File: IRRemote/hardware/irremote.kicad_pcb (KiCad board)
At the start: 2 copper layers, 52.1 x 29.8 mm, 34 parts, among them P2 TL1838_PINHEADER, P3 DS18B20_PINHEADER_TO92, P4 CONN_02X04, P5 CONN_01X04, P6 CONN_01X05, P7 CONN_01X04, P8 TEMP6000, P9 CONN_01X02, Q1 Q_NPN_BEC (MMBT2222ALT1G, 145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, Q2 Q_NPN_BEC (MMBT2222ALT1G, 145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

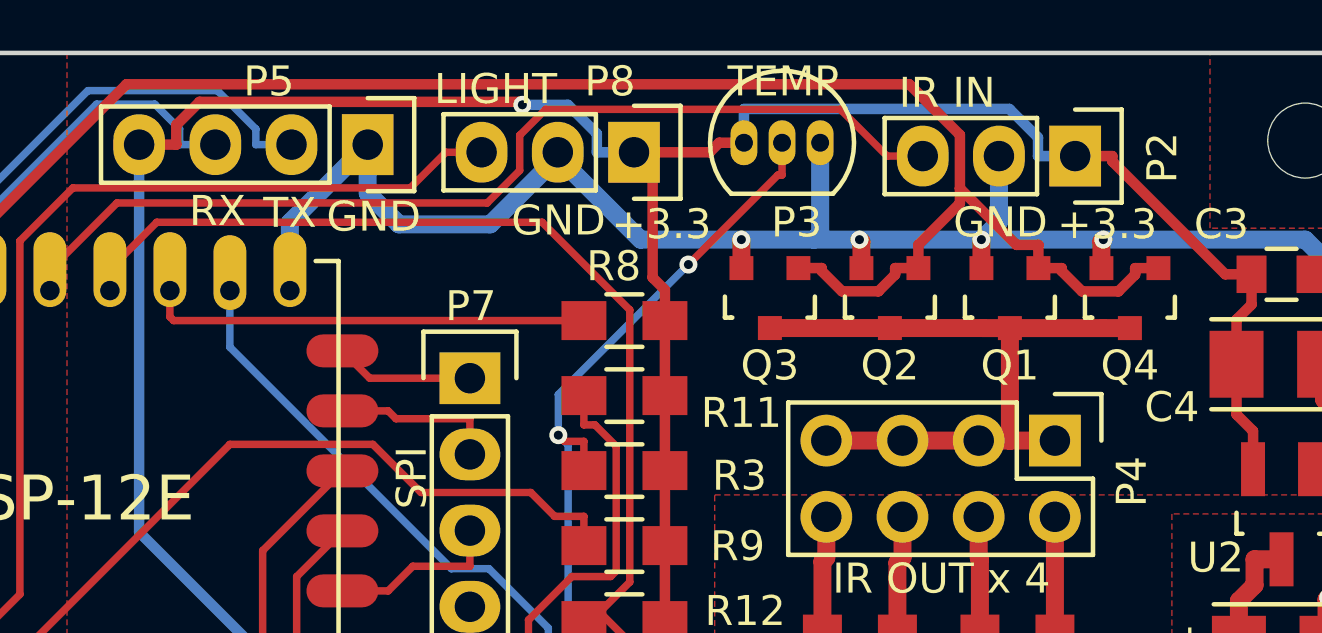
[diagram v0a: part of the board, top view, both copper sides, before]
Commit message: beefed up the led connections a bit
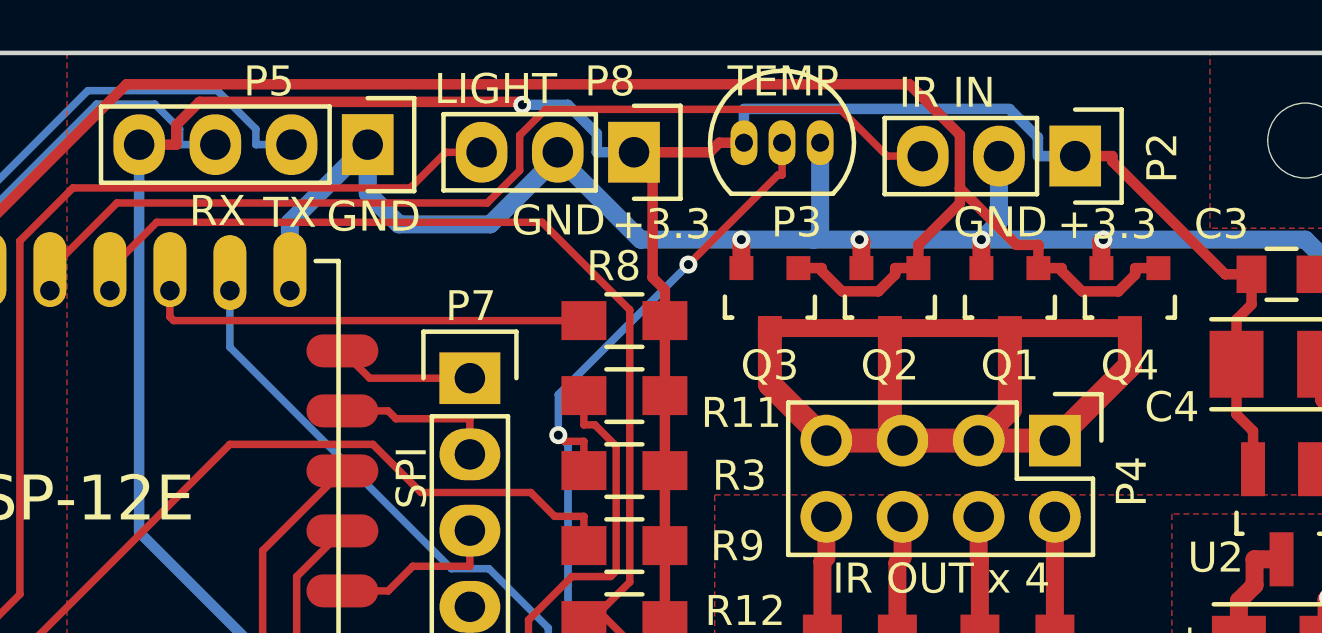
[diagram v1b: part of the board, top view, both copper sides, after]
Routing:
- net LED_DR_5: track 23.4 -> 37.0 mm
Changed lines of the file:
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@@
     (thickness 1.6)
     (drawings 31)
-    (tracks 307)
+    (tracks 313)
     (zones 0)
     (modules 34)
@@
   )
   (setup
-    (last_trace_width 0.25)
+    (last_trace_width 0.8)
     (user_trace_width 0.2)
     (user_trace_width 0.3)
@@
     (effects (font (size 1 1) (thickness 0.25)))
   )
-  (gr_text GND (at 146.685 58.2295 360) (layer F.SilkS)
+  (gr_text GND (at 146.685 58.2295) (layer F.SilkS)
     (effects (font (size 1 1) (thickness 0.25)))
   )
@@
     (effects (font (size 1 1) (thickness 0.25)))
   )
-  (gr_text GND (at 125.7935 58.039 360) (layer F.SilkS)
+  (gr_text GND (at 125.7935 58.039) (layer F.SilkS)
     (effects (font (size 1 1) (thickness 0.25)))
   )
@@
     (effects (font (size 1 1) (thickness 0.25)))
   )
-  (gr_text TX (at 122.9995 57.912 360) (layer F.SilkS)
+  (gr_text TX (at 122.9995 57.912) (layer F.SilkS)
     (effects (font (size 1 1) (thickness 0.25)))
   )
-  (gr_text RX (at 120.5865 57.8485 360) (layer F.SilkS)
+  (gr_text RX (at 120.5865 57.8485) (layer F.SilkS)
     (effects (font (size 1 1) (thickness 0.25)))
   )
@@
   (segment (start 145.334 57.0915) (end 147.2182 58.9757) (width 0.35) (layer F.Cu) (net 6))
   (segment (start 147.95 59.751) (end 147.95 58.9757) (width 0.35) (layer F.Cu) (net 6))
+  (segment (start 139 61.74822) (end 139 63.62) (width 0.8) (layer F.Cu) (net 7))
+  (segment (start 139 63.62) (end 140.88 65.5) (width 0.8) (layer F.Cu) (net 7))
+  (segment (start 151 61.75002) (end 151 63) (width 0.8) (layer F.Cu) (net 7))
+  (segment (start 151 63) (end 148.5 65.5) (width 0.8) (layer F.Cu) (net 7))
+  (segment (start 145.96 65.5) (end 148.5 65.5) (width 0.8) (layer F.Cu) (net 7))
+  (segment (start 143.42 65.5) (end 145.96 65.5) (width 0.8) (layer F.Cu) (net 7))
+  (segment (start 140.88 65.5) (end 143.42 65.5) (width 0.8) (layer F.Cu) (net 7))
+  (segment (start 143 61.74822) (end 143 65.08) (width 0.8) (layer F.Cu) (net 7))
+  (segment (start 143 65.08) (end 143.42 65.5) (width 0.8) (layer F.Cu) (net 7))
+  (segment (start 147 61.75002) (end 147 64.46) (width 0.8) (layer F.Cu) (net 7))
+  (segment (start 147 64.46) (end 145.96 65.5) (width 0.8) (layer F.Cu) (net 7))
   (segment (start 139 61.7482) (end 143 61.7482) (width 0.6) (layer F.Cu) (net 7))
   (segment (start 146.0978 61.7482) (end 146.0996 61.75) (width 0.6) (layer F.Cu) (net 7))
   (segment (start 143 61.7482) (end 146.0978 61.7482) (width 0.6) (layer F.Cu) (net 7))
   (segment (start 147 61.75) (end 146.0996 61.75) (width 0.6) (layer F.Cu) (net 7))
-  (segment (start 145.96 65.5) (end 147 65.5) (width 0.6) (layer F.Cu) (net 7))
-  (segment (start 147 65.5) (end 148.5 65.5) (width 0.6) (layer F.Cu) (net 7))
-  (segment (start 147 65.5) (end 147 61.75) (width 0.6) (layer F.Cu) (net 7))
   (segment (start 151 61.75) (end 150.0996 61.75) (width 0.6) (layer F.Cu) (net 7))
   (segment (start 147 61.75) (end 150.0996 61.75) (width 0.6) (layer F.Cu) (net 7))
-  (segment (start 140.88 65.5) (end 143.42 65.5) (width 0.6) (layer F.Cu) (net 7))
-  (segment (start 143.42 65.5) (end 145.96 65.5) (width 0.6) (layer F.Cu) (net 7))
   (segment (start 148.5 68.04) (end 148.5 72.05) (width 0.6) (layer F.Cu) (net 8))
   (segment (start 146 69.4439) (end 146 72.05) (width 0.6) (layer F.Cu) (net 9))

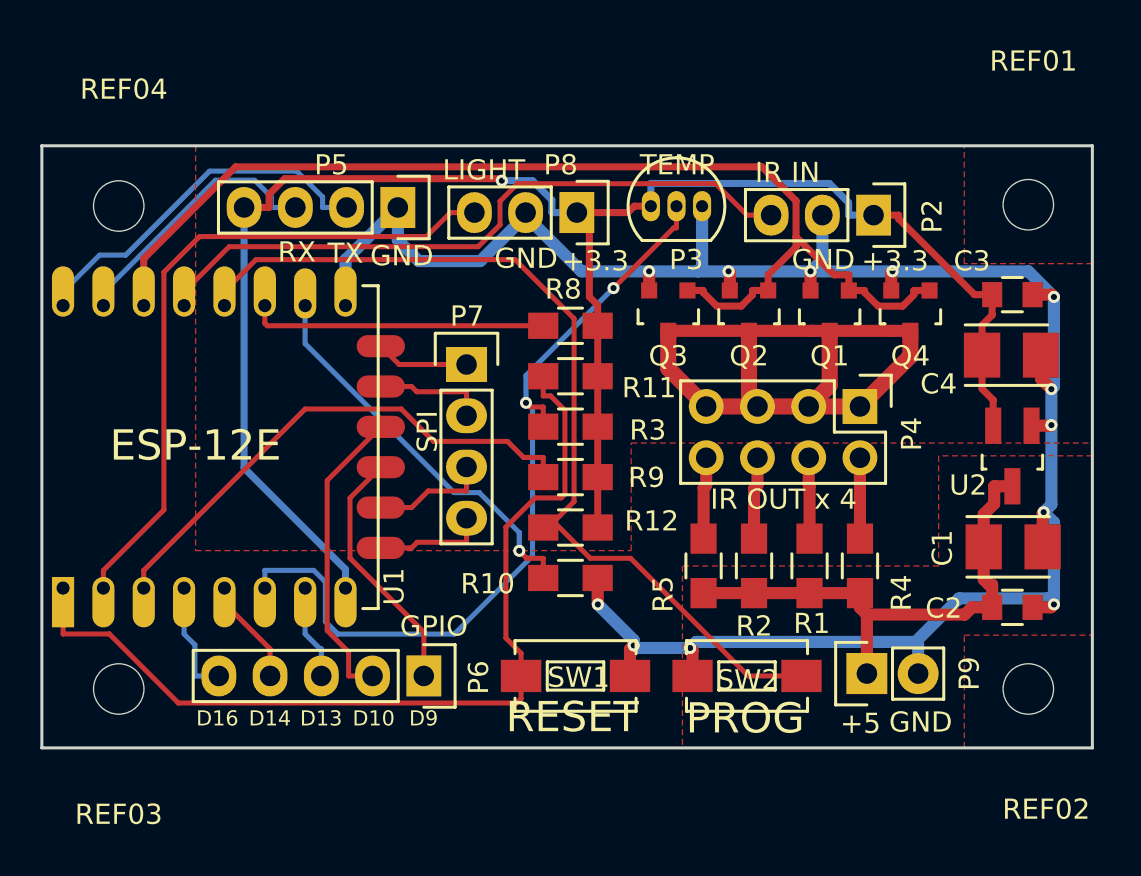
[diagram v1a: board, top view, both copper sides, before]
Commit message: updated board for correct SMD push buttons
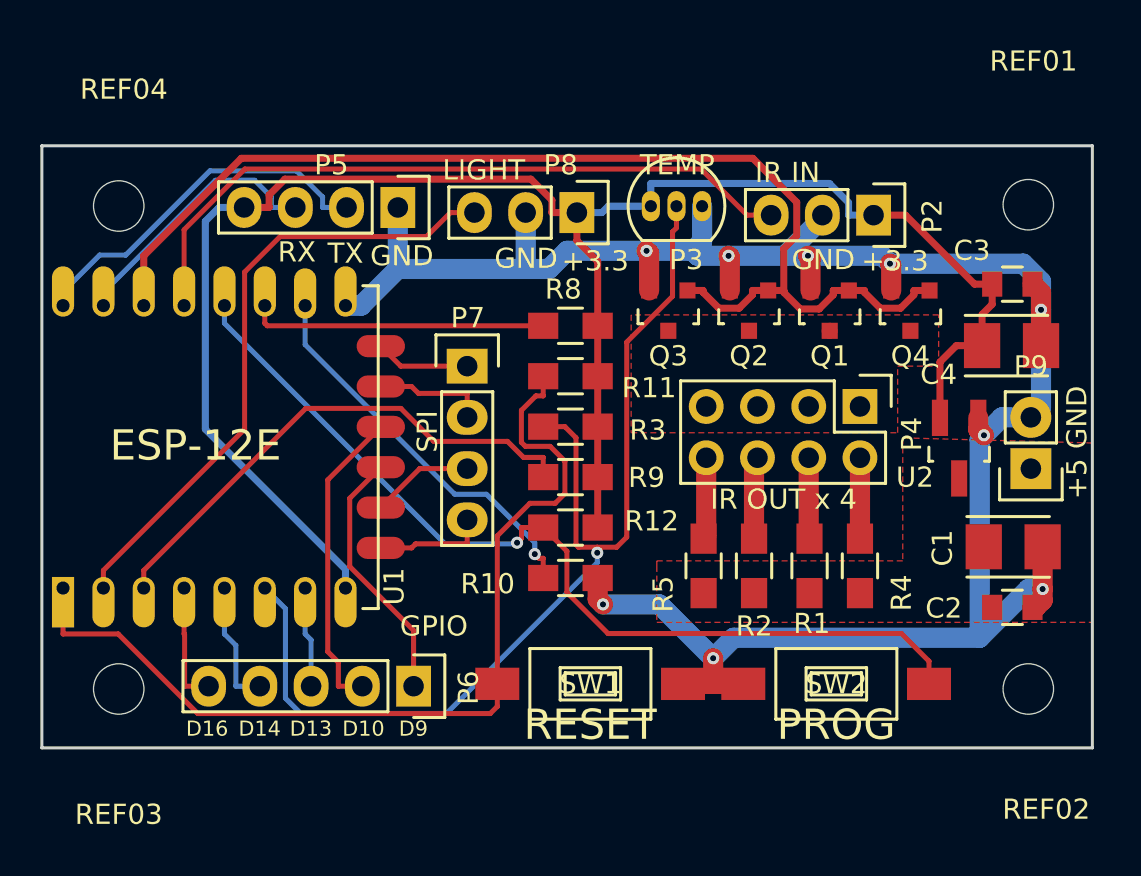
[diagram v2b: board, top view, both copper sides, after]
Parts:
- SW1, SW2: footprint Buttons_Switches_SMD:SW_SPST_EVQPE1 -> Buttons_Switches_SMD:SW_SPST_FSMSM
- moved P9 13.0 mm to (157.0, 68.6), turned to 180 degrees
- moved SW2 4.44 mm to (147.3, 79.2)
- moved U2 2.67 mm to (153.4, 67.6)
- moved SW1 0.82 mm to (135.1, 79.2)
- moved P6 0.72 mm to (126.4, 79.4)
- moved C3 0.52 mm to (156.1, 59.4)
- moved C4 0.47 mm to (156.0, 62.5)
- moved P7 0.09 mm to (129.0, 63.5)
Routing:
- net LED_DR_5: track 37.0 -> 0.00 mm
- net +5V: track 25.6 -> 0.00 mm
- net TEMP_READ: track 40.8 -> 52.9 mm, vias 2 -> 1
- net GND: track 106.7 -> 111.4 mm, vias 12 -> 9
- net +3V3: track 86.8 -> 90.5 mm, vias 1 -> 0
- net TEMT: track 33.5 -> 31.2 mm
- net IR_IN: track 33.3 -> 35.0 mm
- net LED_DR: track 56.1 -> 57.1 mm
- net Net-(P6-Pad4): track 5.29 -> 6.29 mm
- net Net-(R8-Pad1): track 45.4 -> 46.3 mm
- net Net-(R12-Pad2): track 46.8 -> 46.0 mm, vias 0 -> 1
- net Net-(P7-Pad3): track 5.78 -> 5.08 mm
- added copper zone on F.Cu, net LED_DR_5
- removed copper zone on F.Cu, net +3V3

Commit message: moved the microusb for power, fixed push button switches, flipped IR receiver
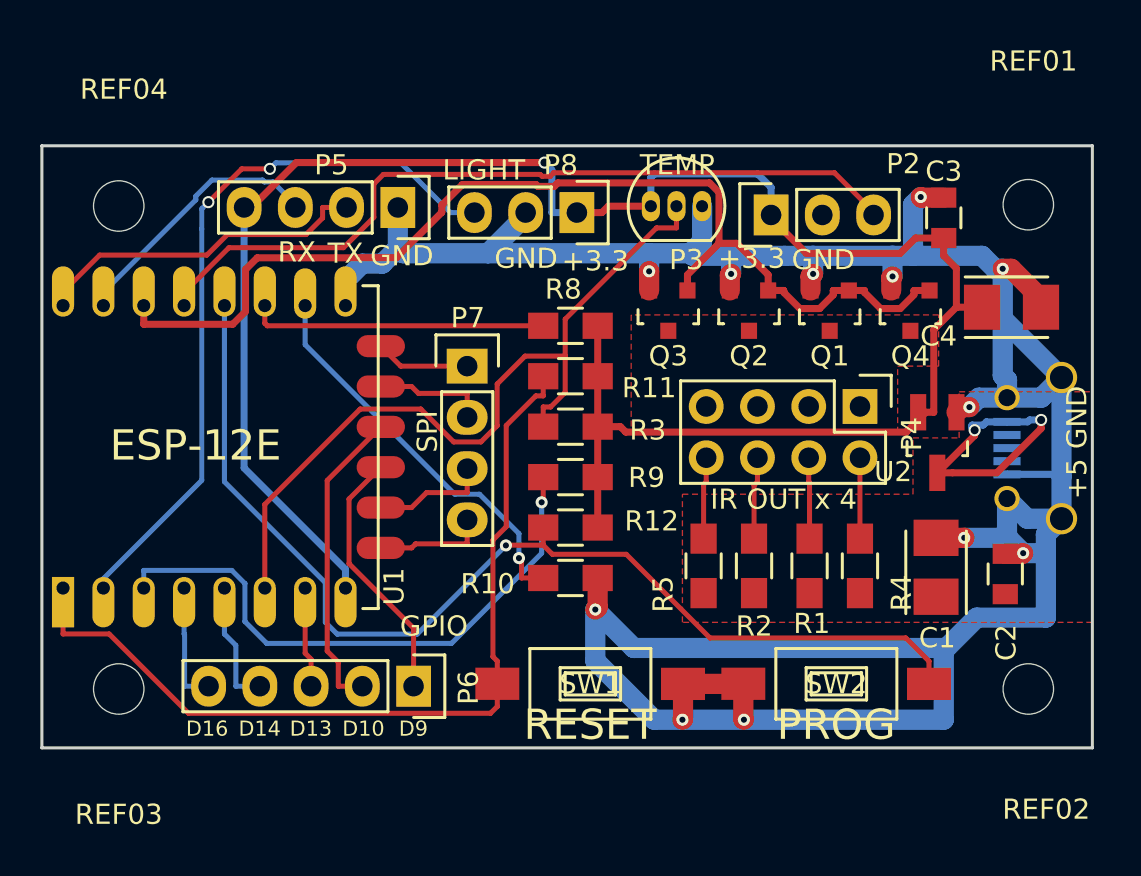
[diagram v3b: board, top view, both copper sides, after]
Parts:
- removed P9: CONN_01X02, Pin_Headers:Pin_Header_Straight_1x02
- added P1: USB_OTG, MyKiCadLibs:USB_Micro-B-OshPark, B.Cu at (157.4, 67.6)
- moved P2 5.08 mm to (144.1, 56.0), turned to 90 degrees
- moved C3 4.73 mm to (152.7, 56.1), turned to 90 degrees
- moved C1 3.95 mm to (152.3, 73.5), turned to 90 degrees
- moved C4 1.91 mm to (156.0, 60.6)
- moved C2 1.69 mm to (155.7, 73.8), turned to 90 degrees
- moved U2 1.12 mm to (152.3, 67.3)
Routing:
- net GND: track 111.4 -> 156.5 mm, vias 9 -> 12
- net TEMP_READ: track 52.9 -> 39.1 mm, vias 1 -> 0
- net +5V: track 0.00 -> 13.7 mm, vias 0 -> 2
- net +3V3: track 90.5 -> 101.5 mm, vias 0 -> 1
- net Net-(R12-Pad2): track 46.0 -> 54.1 mm
- net TEMT: track 31.2 -> 36.3 mm, vias 0 -> 2
- net IR_IN: track 35.0 -> 39.3 mm
- net LED_DR: track 57.1 -> 53.3 mm
- net Net-(R8-Pad1): track 46.3 -> 43.3 mm
- net Net-(R9-Pad1): track 26.0 -> 28.9 mm, vias 0 -> 1
- net RXD_UA_1: track 18.3 -> 16.8 mm
- net Net-(P7-Pad3): track 5.08 -> 5.78 mm
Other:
- board text removed: "IR IN"

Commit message: update oshpark link
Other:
- board text added: "IR In"
- board text removed: "+5"
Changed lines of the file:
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@@
     (links 77)
     (no_connects 0)
-    (area 89.666424 39.630625 175.259 86.7)
+    (area 89.666424 42.87 175.259 86.7)
     (thickness 1.6)
-    (drawings 30)
+    (drawings 29)
     (tracks 364)
     (zones 0)
@@
     (descr "Through hole pin header")
     (tags "pin header")
-    (fp_text reference P2 (at 2.531 6.554 180) (layer F.SilkS)
+    (fp_text reference P2 (at -0.635 7.035 270) (layer F.SilkS)
       (effects (font (size 1 1) (thickness 0.15)))
     )
@@
       (net 1 GND))
   )
+  (gr_text "IR In" (at 149.225 53.721) (layer F.SilkS)
+    (effects (font (size 1 1) (thickness 0.25)))
+  )
   (dimension 52.07 (width 0.3) (layer Cmts.User)
     (gr_text "52.070 mm" (at 133.985 44.37) (layer Cmts.User)
@@
     (effects (font (size 1 1) (thickness 0.25)))
   )
-  (gr_text TEMP (at 139.446 53.5305) (layer F.SilkS)
+  (gr_text TEMP (at 139.446 53.721) (layer F.SilkS)
     (effects (font (size 1 1) (thickness 0.25)))
   )
-  (gr_text GND (at 159.258 66.04 90) (layer F.SilkS)
-    (effects (font (size 1 1) (thickness 0.25)))
-  )
-  (gr_text +5 (at 159.258 69.088 90) (layer F.SilkS)
-    (effects (font (size 1 1) (thickness 0.25)))
-  )

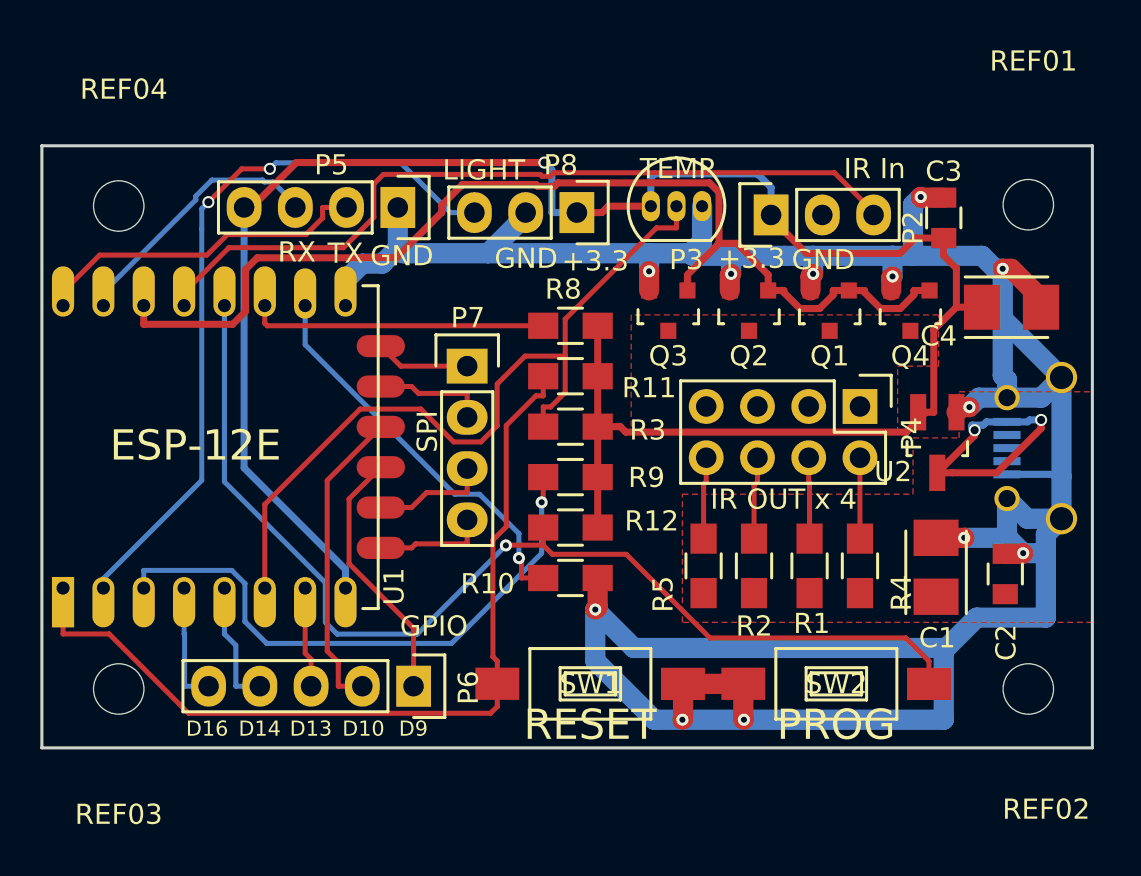
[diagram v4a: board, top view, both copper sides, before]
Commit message: updated oshpark link
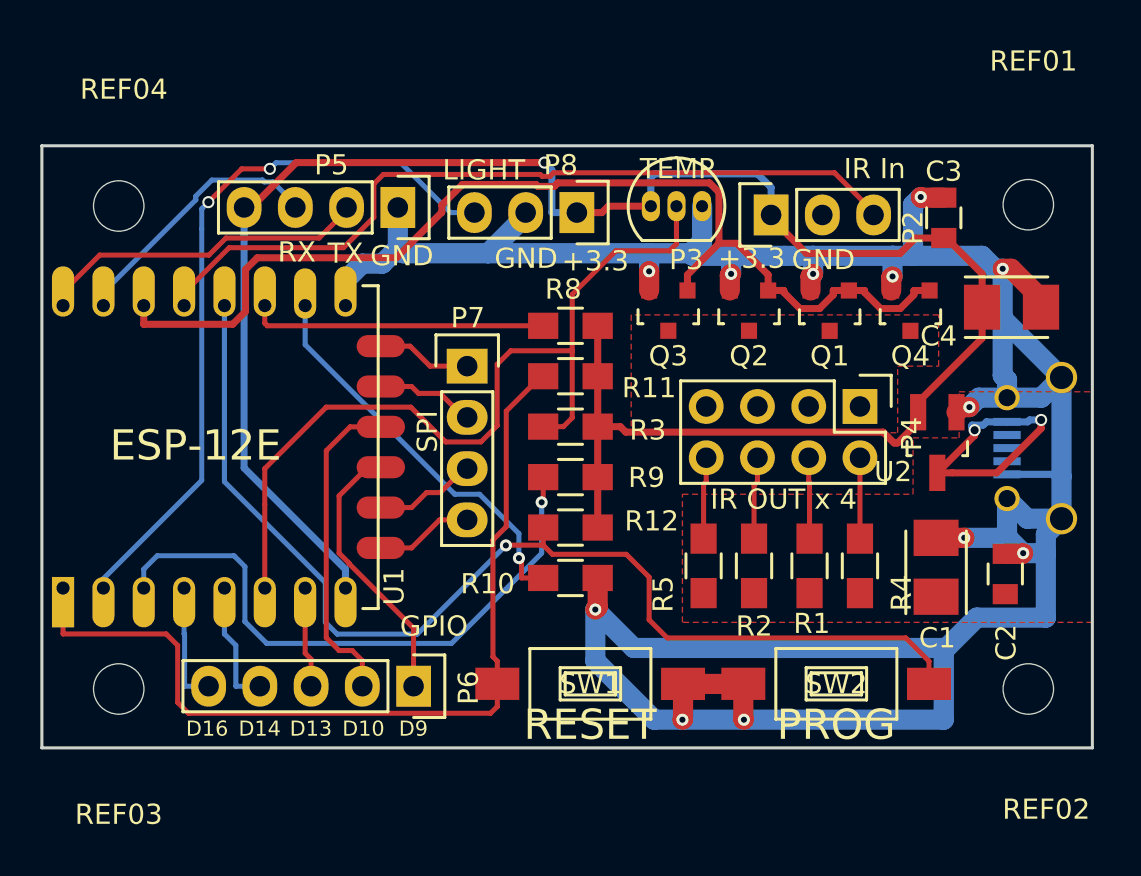
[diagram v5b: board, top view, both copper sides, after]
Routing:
- net TEMP_READ: track 39.1 -> 42.7 mm
- net Net-(R8-Pad1): track 43.3 -> 44.8 mm
- net Net-(R12-Pad2): track 54.1 -> 55.4 mm
- net Net-(R9-Pad1): track 28.9 -> 30.0 mm
- net Net-(P6-Pad1): track 12.8 -> 13.6 mm
- net Net-(P7-Pad3): track 5.78 -> 5.08 mm
- net Net-(P7-Pad2): track 5.61 -> 4.92 mm
- net Net-(P7-Pad4): track 5.55 -> 4.86 mm
- net Net-(P6-Pad2): track 15.4 -> 16.0 mm
